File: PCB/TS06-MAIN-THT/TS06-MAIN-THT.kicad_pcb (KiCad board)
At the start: 2 copper layers, 176 x 96 mm, 152 parts, among them J1 PH 6, U1 Arduino Nano, U10 TLP627, U11 TC4420, U12 LM393, U13 DS3231 mini, U14 R-78E5.0-1.0, U2 K155ID1, U3 MCP23017, U4 MCP23017, U5 TLP627, U6 TLP627, U7 TLP627, U8 TLP627, U9 TLP627

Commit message: PCB: route TS06-MAIN; the router learns what has to be laid before what
The surface-mount build routes: 3047 tracks, 476 vias, every net connected except one
base pin. KiCad's own DRC with zones refilled reports 17 items, of which 2 are that net
and the rest are accepted (the tubes' pip holes inside their own courtyards, four
silkscreen warnings, the colon lamps touching the M10 glass courtyard by 0.3 mm).
checkmatch agrees the board and its schematic connect the same things.

ROUTING ORDER is the whole of it, and most of this diff is the evidence. Stages are now:
high voltage including the 185 V trunk, then GND as a tree, then everything else
negotiated, then one more try alone at whatever was dropped. What was tried and is worse
is written into tools/mkpcb_main.py beside each decision, with the numbers:

  * GND negotiated with the signals - it is 74 of 483 pads, so nearly every net is
    reported as overlapping GND rather than its real neighbour; two runs stuck at ~80 of
    98 nets overlapping and could not converge.
  * GND as a pour with stubs - the signal copper cuts the pour into islands; one region
    reached 37 of 74 pads and 66 stubs could not close the rest.
  * GND after the signals - the board is full by then; 21 pads unreachable, GND in
    11 pieces. Before them it wires with 0 or 1 connection missing.
  * The cathode spine laid first like the trunk - laid net after net it fences the rest
    in: 6 nets dropped instead of 3. Negotiation beats ordering, as TS06-SEC says.
  * AM/PM switches moved out of the tube rings - their 18 collectors then come back in
    through the ring edge with 0.6 mm halos and choke it: 24 nets dropped, and 13 when
    only the three with stranded pins were moved.

tools/pcbroute.py: negotiate() keeps its BEST round, not its last. price * cnt * (1 +
hist) saturates the int32 cap once the price has climbed far enough, and from there the
cost landscape is flat and the count wanders upward - 11, 12, 13, 17 over four rounds on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
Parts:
- moved ? 186.1 mm to (6.00, 90.0)
- moved ? 165.0 mm to (170.0, 90.0)
- moved C1 99.7 mm to (162.5, 5.40)
- moved VT12 82.6 mm to (129.0, 81.3)
- moved ? 81.0 mm to (90.0, 89.5)
- moved VT17 78.8 mm to (129.0, 87.3)
- moved VT18 77.9 mm to (138.0, 87.3)
- moved VT19 77.1 mm to (146.9, 87.3)
- moved R56 75.0 mm to (165.8, 40.6)
- moved VT16 71.7 mm to (164.8, 81.3)
- moved R54 71.2 mm to (170.0, 38.8)
- moved VT15 70.9 mm to (155.8, 81.3)
- moved VT14 70.3 mm to (146.9, 81.3)
- moved ? 70.1 mm to (83.0, 22.0)
- moved VT13 69.8 mm to (138.0, 81.3)
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
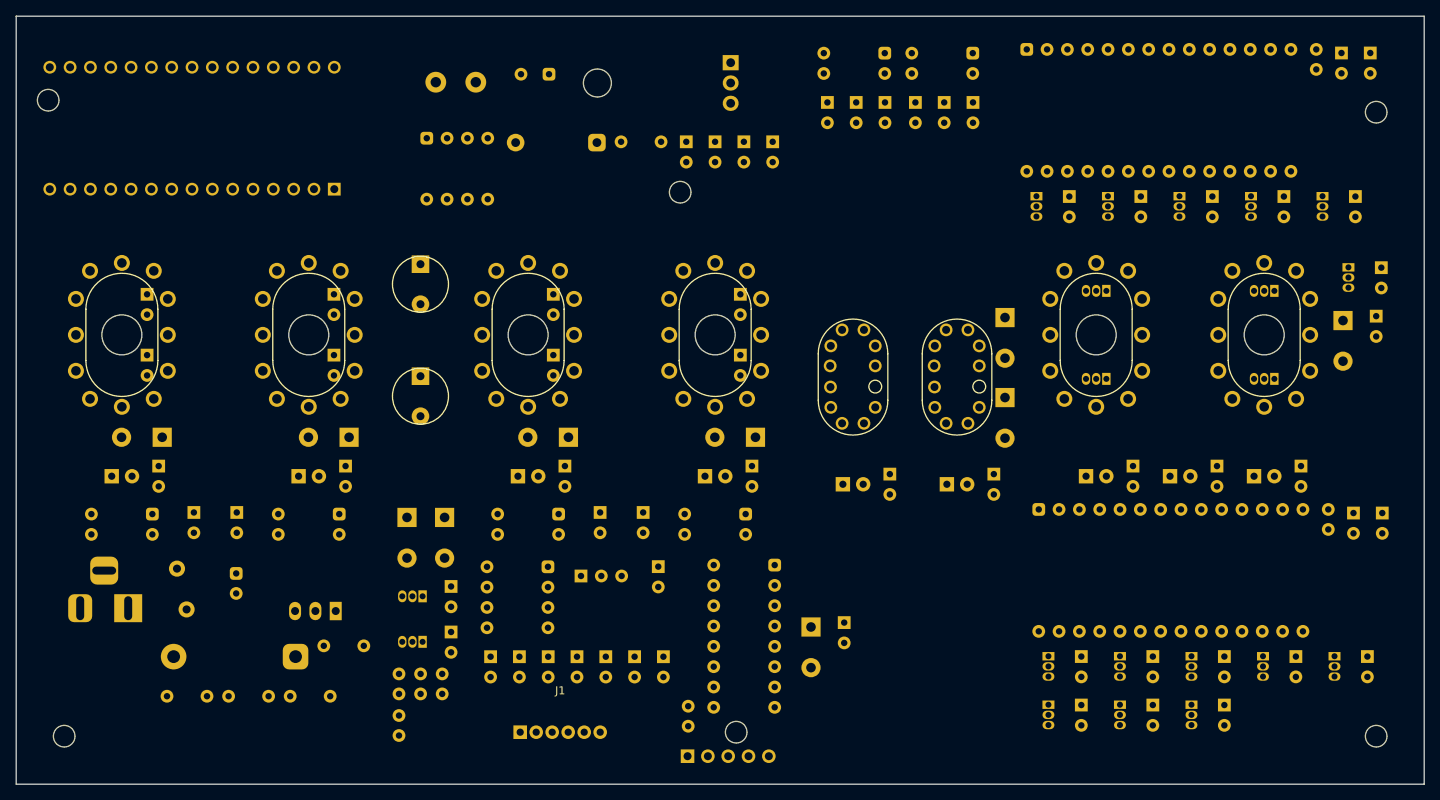
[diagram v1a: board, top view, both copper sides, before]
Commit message: PCB/README: the routing results for both TS06-MAIN builds, and what is left
The surface-mount build routes with one net unconnected and KiCad DRC clean apart from
that and three accepted items. The through-hole build is space-limited and needs its own
placement pass: 13 split nets and 50 through-hole pads inside another part CourtYard.
Both tables, the one known surface-mount defect and why moving the in-ring switches is
not its fix, are written up beside the decisions that produced them.

Co-Authored-By: Claude Opus 5 <noreply@anthropic.com>
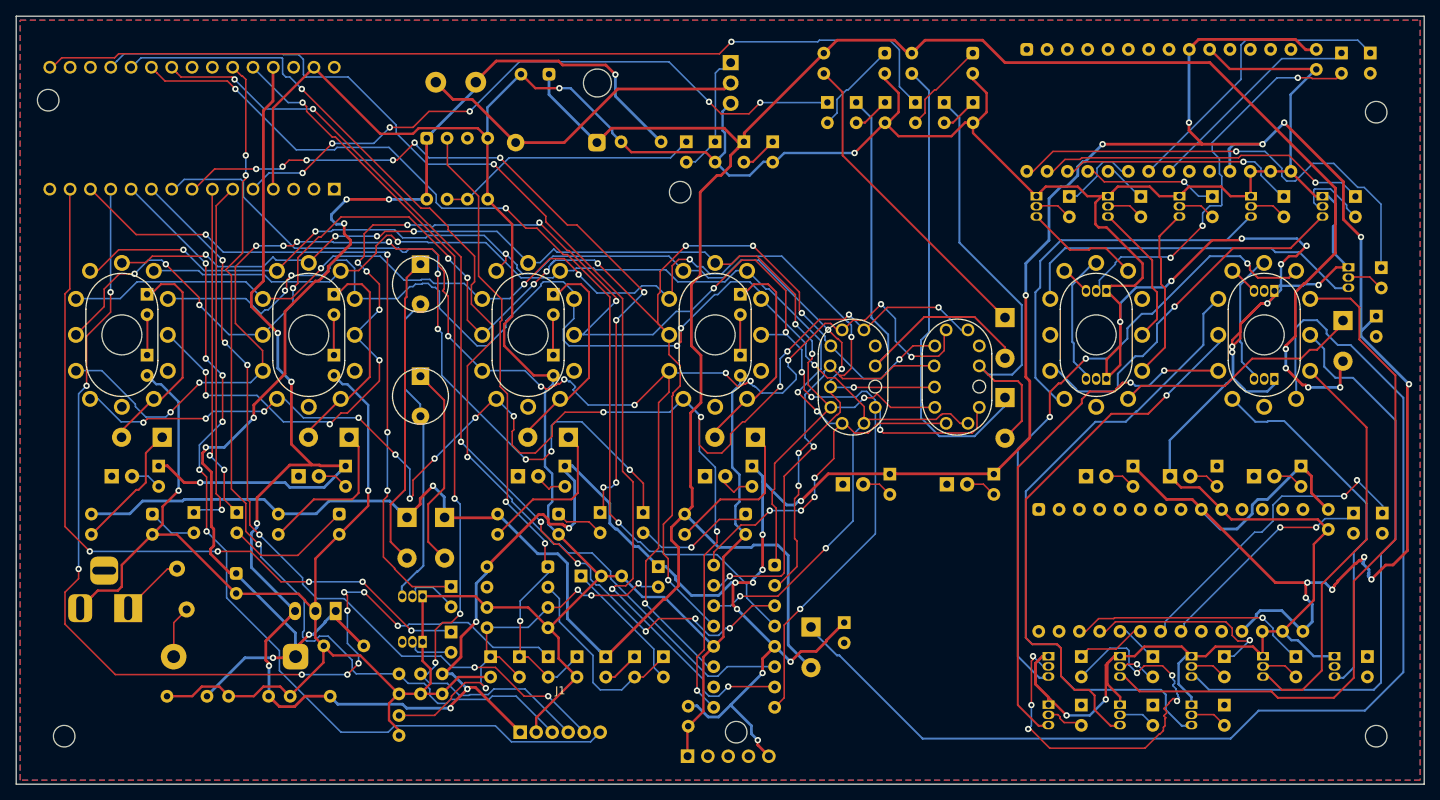
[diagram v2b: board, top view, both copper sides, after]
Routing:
- net GND: track 0.00 -> 841.8 mm, vias 0 -> 15
- net +5V: track 0.00 -> 587.1 mm, vias 0 -> 30
- net HV185: track 0.00 -> 345.1 mm, vias 0 -> 5
- net K9: track 0.00 -> 220.6 mm, vias 0 -> 16
- net K2: track 0.00 -> 210.4 mm, vias 0 -> 16
- net K3: track 0.00 -> 205.7 mm, vias 0 -> 14
- net K1: track 0.00 -> 195.3 mm, vias 0 -> 17
- net K4: track 0.00 -> 178.2 mm, vias 0 -> 7
- net K8: track 0.00 -> 176.7 mm, vias 0 -> 7
- net K5: track 0.00 -> 159.5 mm, vias 0 -> 8
- net +12V: track 0.00 -> 158.8 mm, vias 0 -> 8
- net K7: track 0.00 -> 151.0 mm, vias 0 -> 7
- net K6: track 0.00 -> 147.0 mm, vias 0 -> 7
- net A0: track 0.00 -> 145.4 mm, vias 0 -> 3
- net ANODE_PM: track 0.00 -> 144.8 mm
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- added copper zone on B.Cu, net GND
- added copper zone on F.Cu, net GND

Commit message: PCB: both TS06-MAIN builds re-routed, and the README says what is now true
Surface-mount: every signal net connected, 339 vias against 476, 49%/11% front grain
against 33%/25%, checkcopper --hv clean, checkmatch agrees. The VT2 base that used to
be the one split net is routed.

Through-hole: the rules improve its copper a lot - 177 vias against 271, a grain of
44/14 where it used to run MORE ACROSS than along - and do not touch its connectivity.
13 nets split either way. That build's problem is placement and always was.

The README now carries the measured trade for the two stranded ИН-15 emitters, the
pointer to the routing study and its twenty-two configurations, and the two findings
that dwarf the routing work: placecheck's 16% of the floor from moving two parts, and
boardsplit's eighteen-wire seam.

Co-Authored-By: Claude Opus 5 <noreply@anthropic.com>
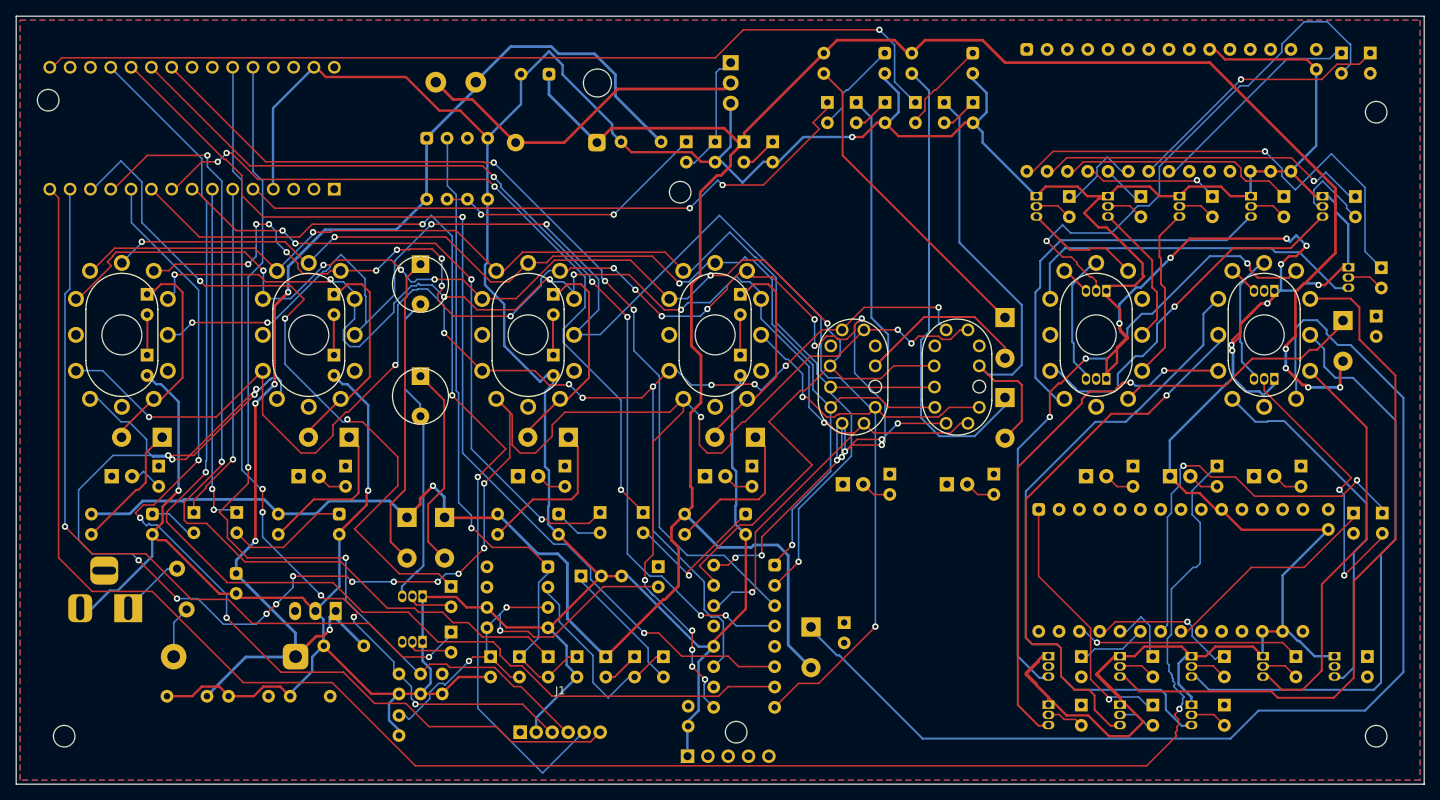
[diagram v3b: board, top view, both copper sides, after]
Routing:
- net +5V: track 587.1 -> 0.00 mm, vias 30 -> 0
- net D12: track 0.00 -> 237.9 mm, vias 0 -> 1
- net K3: track 205.7 -> 0.00 mm, vias 14 -> 0
- net K1: track 195.3 -> 282.6 mm, vias 17 -> 23
- net B12: track 56.1 -> 0.00 mm, vias 6 -> 0
- net K7: track 151.0 -> 195.8 mm, vias 7 -> 24
- net B11: track 0.00 -> 37.2 mm, vias 0 -> 2
- net U4_GPB0: track 0.00 -> 33.5 mm, vias 0 -> 1
- net D7: track 100.2 -> 124.3 mm, vias 6 -> 3
- net GND: track 841.8 -> 863.0 mm, vias 15 -> 12
- net D9: track 135.5 -> 114.7 mm, vias 10 -> 2
- net K2: track 210.4 -> 191.2 mm, vias 16 -> 10
- net B2: track 50.0 -> 67.8 mm, vias 3 -> 1
- net D5: track 97.1 -> 81.3 mm, vias 10 -> 4
- net U4_GPA1: track 39.6 -> 51.5 mm
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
